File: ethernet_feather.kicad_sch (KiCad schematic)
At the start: 13 parts

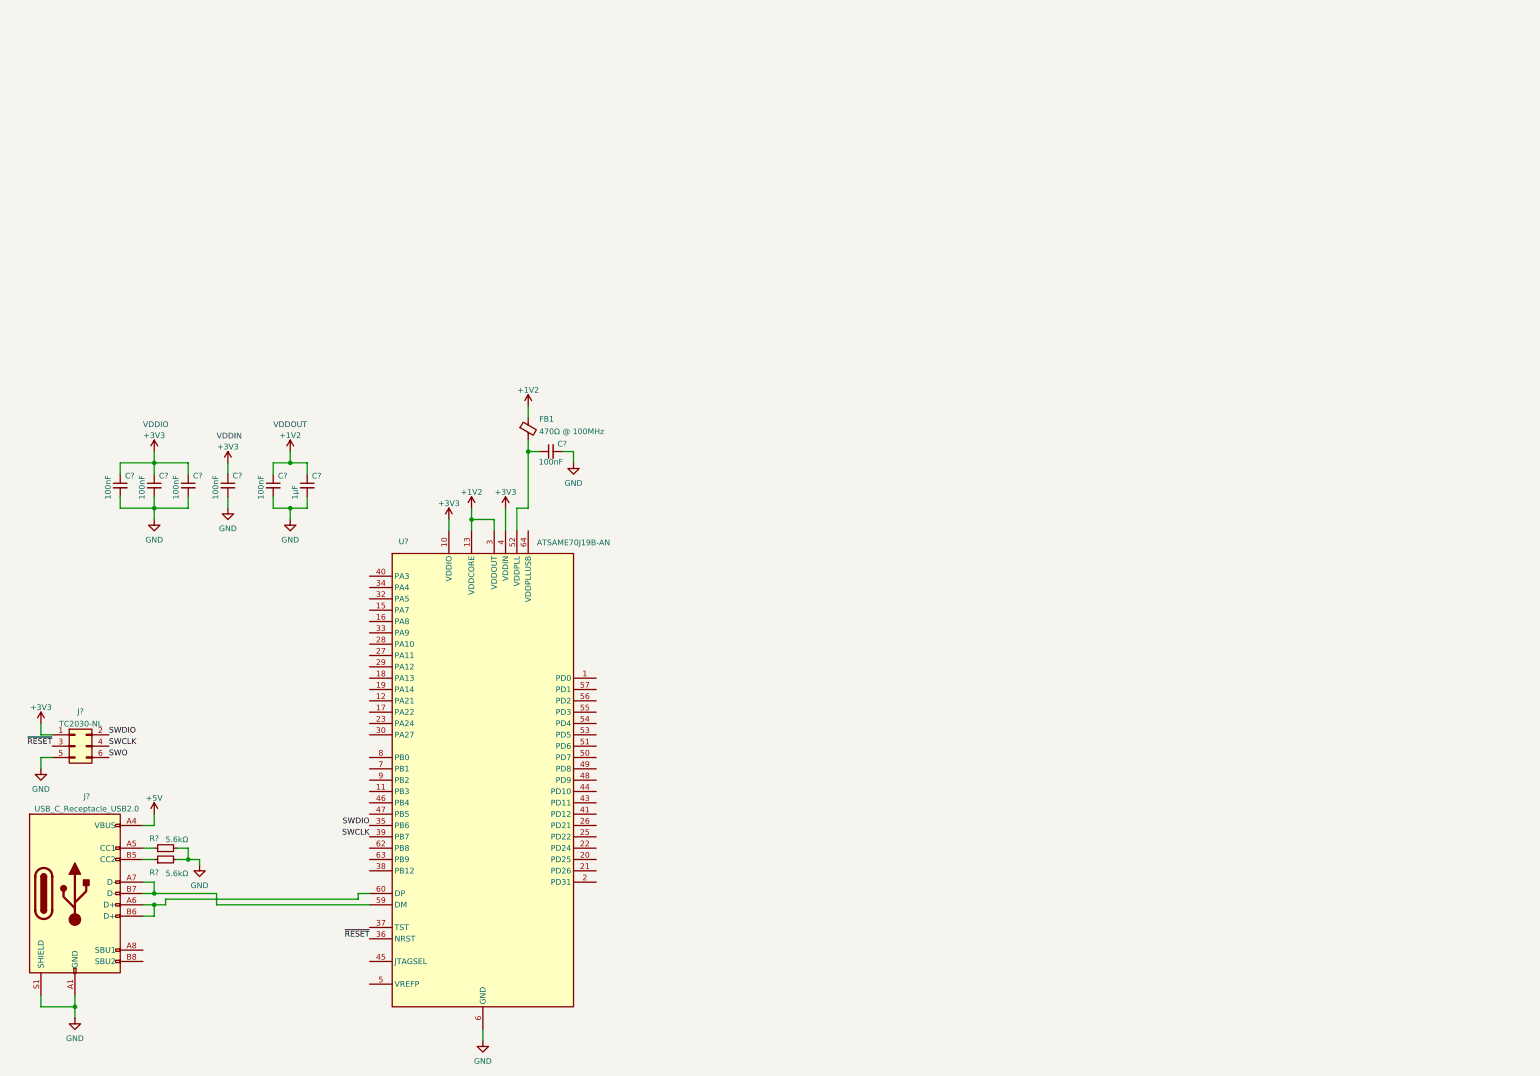
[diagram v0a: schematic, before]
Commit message: Add crystals
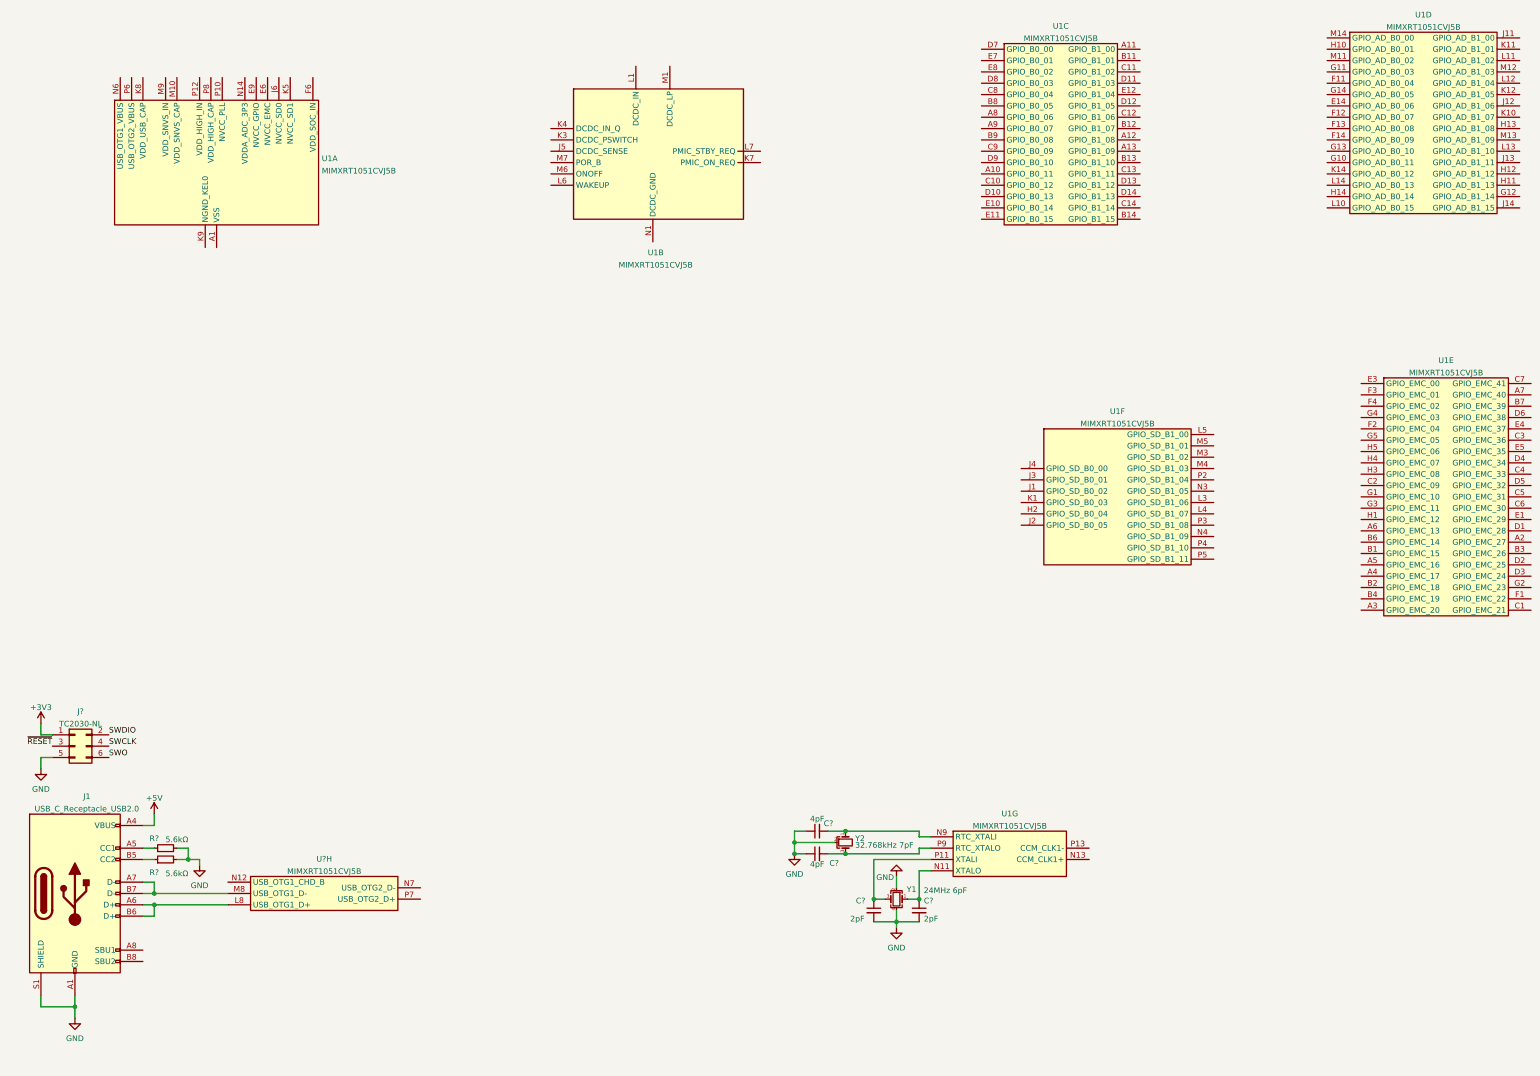
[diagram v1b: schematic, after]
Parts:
- removed C? (x6): 100nF, symbol Device:C_Small
- removed C?: 1µF, symbol Device:C_Small
- removed FB1: 470Ω @ 100MHz, symbol Device:FerriteBead_Small
- removed U?: ATSAME70J19B-AN, Package_QFP:LQFP-64_10x10mm_P0.5mm, symbol MCU_Microchip_SAME:ATSAME70J19A-AN
- added C? (x2): 4pF, symbol Device:C_Small
- added C? (x2): 2pF, Capacitor_SMD:C_0603_1608Metric, symbol Device:C_Small
- added U1, U?: MIMXRT1051CVJ5B, symbol ethernet_feather:MIMXRT1051CVJ5B
- added Y1: 24MHz 6pF, Crystal:Crystal_SMD_2016-4Pin_2.0x1.6mm, symbol Device:Crystal_GND24_Small
- added Y2: 32.768kHz 7pF, Crystal:Crystal_SMD_MicroCrystal_MS3V-T1R, symbol Device:Crystal_GND2_Small
- gave numbers to parts that had none: 1
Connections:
- net GND: now also C?.1, C?.1, C?.2, C?.2, Y1.2, Y1.4, Y2.2
- net at J1.A6 (D+), J1.B6 (D+): now also U?.L8 (USB_OTG1_D+)
- net at J1.A7 (D-), J1.B7 (D-): now also U?.M8 (USB_OTG1_D-)
- new net: C?.1, U1.N11 (XTALO), Y1.1
- new net: C?.2, U1.N9 (RTC_XTALI), Y2.1
- new net: C?.1, U1.P11 (XTALI), Y1.3
- new net: C?.2, U1.P9 (RTC_XTALO), Y2.3
- new net: U1.M1 (DCDC_LP), U1.M2 (DCDC_LP)
- new net DCDC_GND: U1.N1 (DCDC_GND), U1.N2 (DCDC_GND)
- new net DCDC_IN: U1.L1 (DCDC_IN), U1.L2 (DCDC_IN)
- new net NVCC_EMC: U1.E6 (NVCC_EMC), U1.F5 (NVCC_EMC)
- new net NVCC_GPIO: U1.E9 (NVCC_GPIO), U1.F10 (NVCC_GPIO), U1.J10 (NVCC_GPIO)
- new net VDD_SOC_IN: U1.F6 (VDD_SOC_IN), U1.F7 (VDD_SOC_IN), U1.F8 (VDD_SOC_IN), U1.F9 (VDD_SOC_IN), U1.G6 (VDD_SOC_IN), U1.G9 (VDD_SOC_IN), U1.H6 (VDD_SOC_IN), U1.H9 (VDD_SOC_IN), U1.J9 (VDD_SOC_IN)
- new net VSS: U1.A1 (VSS), U1.A14 (VSS), U1.B10 (VSS), U1.B5 (VSS), U1.E13 (VSS), U1.E2 (VSS), U1.G7 (VSS), U1.G8 (VSS), U1.H7 (VSS), U1.H8 (VSS), U1.J7 (VSS), U1.J8 (VSS), U1.K13 (VSS), U1.K2 (VSS), U1.L9 (VSS), U1.N5 (VSS), U1.N8 (VSS), U1.P1 (VSS), U1.P14 (VSS)
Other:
- note removed: "VDDIN"
- note removed: "VDDIO"
- note removed: "VDDOUT"

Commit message: Most of the HV side captured
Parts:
- added A1: Adafruit_Feather_Generic, Module:Adafruit_Feather, symbol MCU_Module:Adafruit_Feather_Generic
- added C? (x9): 100nF, symbol Device:C_Small
- added C? (x4): 4.7µF, symbol Device:C_Small
- added C?: 1µF, symbol Device:C_Small
- added C?: 220nF, symbol Device:C_Small
- added C?: C_Small, symbol Device:C_Small
- added H1, H2: 0.1", MountingHole:MountingHole_2.5mm_Pad, symbol Mechanical:MountingHole_Pad
- added H3, H4: 0.1", MountingHole:MountingHole_2.5mm, symbol Mechanical:MountingHole
- added J?: Conn_02x02_Odd_Even, symbol Connector_Generic:Conn_02x02_Odd_Even
- added J?: RJ45_Abracon_ARJM11D7-114-AB-EW2, ethernet_feather:RJ45_Abracon_ARJM11D7-114, symbol ethernet_feather:RJ45_Abracon_ARJM11D7-114-AB-EW2
- added U?: WE-TVS-82400102, Package_TO_SOT_SMD:SOT-23-6, symbol Power_Protection:WE-TVS-82400102
- added U?: W25Q32JVZP, Package_SON:WSON-8-1EP_6x5mm_P1.27mm_EP3.4x4.3mm, symbol Memory_Flash:W25Q32JVZP
- C3, C4: renamed from C?; footprint (none) -> Capacitor_SMD:C_0603_1608Metric
- J1: footprint (none) -> Connector_USB:USB_C_Receptacle_HRO_TYPE-C-31-M-12
- R1, R2: renamed from R?; footprint (none) -> Resistor_SMD:R_0603_1608Metric
- U1: footprint (none) -> ethernet_feather:LFBGA-196_12x12mm_Layout14x14_P0.8mm
- U1: renamed from U?; footprint (none) -> ethernet_feather:LFBGA-196_12x12mm_Layout14x14_P0.8mm
- gave numbers to parts that had none: 3
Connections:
- net NVCC_EMC is gone; now on net +3V3: U1.E6 (NVCC_EMC), U1.F5 (NVCC_EMC)
- net NVCC_GPIO is gone; now on net +3V3: U1.E9 (NVCC_GPIO), U1.F10 (NVCC_GPIO), U1.J10 (NVCC_GPIO)
- net VSS is gone; now on net GND: U1.A1 (VSS), U1.A14 (VSS), U1.B10 (VSS), U1.B5 (VSS), U1.E13 (VSS), U1.E2 (VSS), U1.G7 (VSS), U1.G8 (VSS), U1.H7 (VSS), U1.H8 (VSS), U1.J7 (VSS), U1.J8 (VSS), U1.K13 (VSS), U1.K2 (VSS), U1.L9 (VSS), U1.N5 (VSS), U1.N8 (VSS), U1.P1 (VSS), U1.P14 (VSS)
- net +3V3: now also U1.J6 (NVCC_SD0), U1.K5 (NVCC_SD1), U1.N14 (VDDA_ADC_3P3), U1.P12 (VDD_HIGH_IN), C?.1, C?.1, C?.1, C?.1, C?.1, C?.1, C?.1, C?.1, C?.1, C?.1, C?.1, C?.1, C?.1, U?.8 (VCC)
- net +5V: now also U?.5
- net GND: now also U1.K9 (NGND_KEL0), C?.1, C?.1, C?.2, C?.2, C?.2, C?.2, C?.2, C?.2, C?.2, C?.2, C?.2, C?.2, C?.2, C?.2, C?.2, H1.1, H2.1, J?.SH (SHIELD), U?.2, U?.4 (GND), U?.9 (EP)
- net SWDIO: now also U1.A8 (GPIO_B0_06)
- net SWO: now also U1.D10 (GPIO_B0_13)
- net ~{RESET}: now also U1.A10 (GPIO_B0_11)
- net SWDCLK: now reaches U1.A9 (GPIO_B0_07)
- net at J1.A6 (D+), J1.B6 (D+): now also U?.6; no longer U1.L8 (USB_OTG1_D+)
- net at J1.A7 (D-), J1.B7 (D-): now also U?.4; no longer U1.M8 (USB_OTG1_D-)
- net at U1.L3 (GPIO_SD_B1_06): now also U?.1 (~{CS})
- net at U1.L4 (GPIO_SD_B1_07): now also U?.6 (CLK)
- net at U1.N4 (GPIO_SD_B1_09): now also U?.2 (DO(IO1))
- net at U1.P3 (GPIO_SD_B1_08): now also U?.5 (DI(IO0))
- net at U1.P4 (GPIO_SD_B1_10): now also U?.3 (IO2)
- net at U1.P5 (GPIO_SD_B1_11): now also U?.7 (IO3)
- new net: C?.2, J?.4 (CT)
- new net: U1.L8 (USB_OTG1_D+), U?.1
- new net: U1.M8 (USB_OTG1_D-), U?.3
- new net: C?.2, J?.9 (V+)
- new net: J?.1 (Pin_1), J?.2 (TD-)
- new net: J?.2 (Pin_2), J?.7
- new net: J?.1 (TD+), J?.3 (Pin_3)
- new net: J?.4 (Pin_4), J?.6 (RD-)
- no-connect marks 0 -> 4
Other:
- moved on the sheet: C1, C2, C3, C4, J1, R1, R2, U1A, U1D, U1F, U1G, U1H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

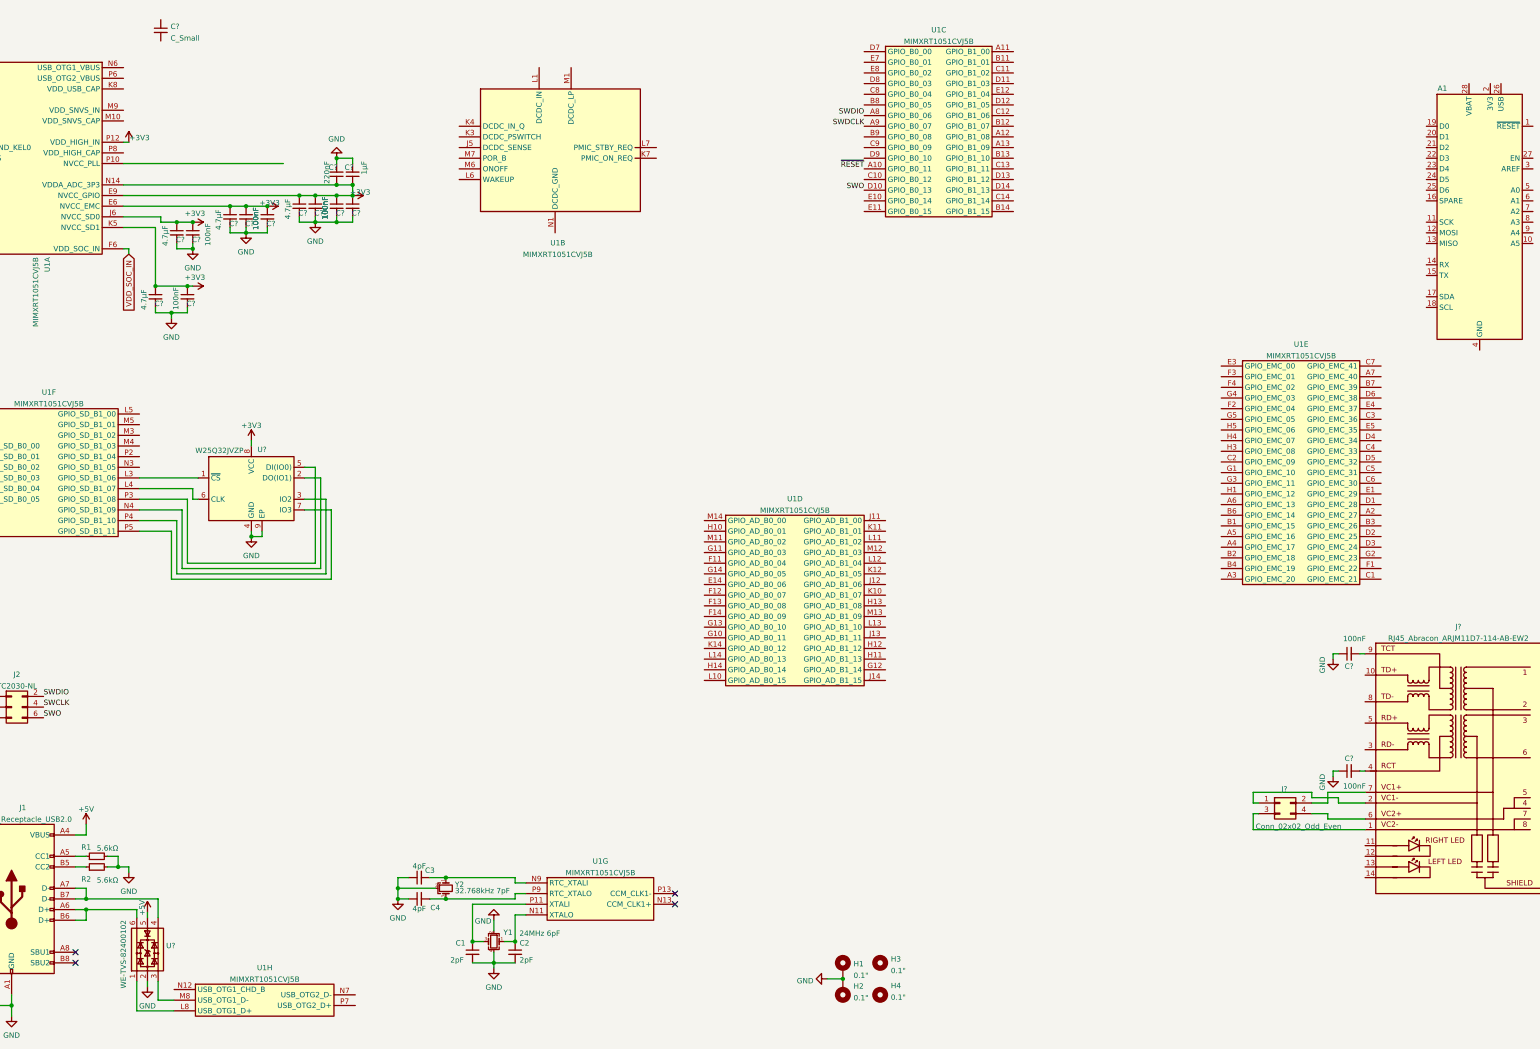
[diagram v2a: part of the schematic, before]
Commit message: Assign footprints and add LDO
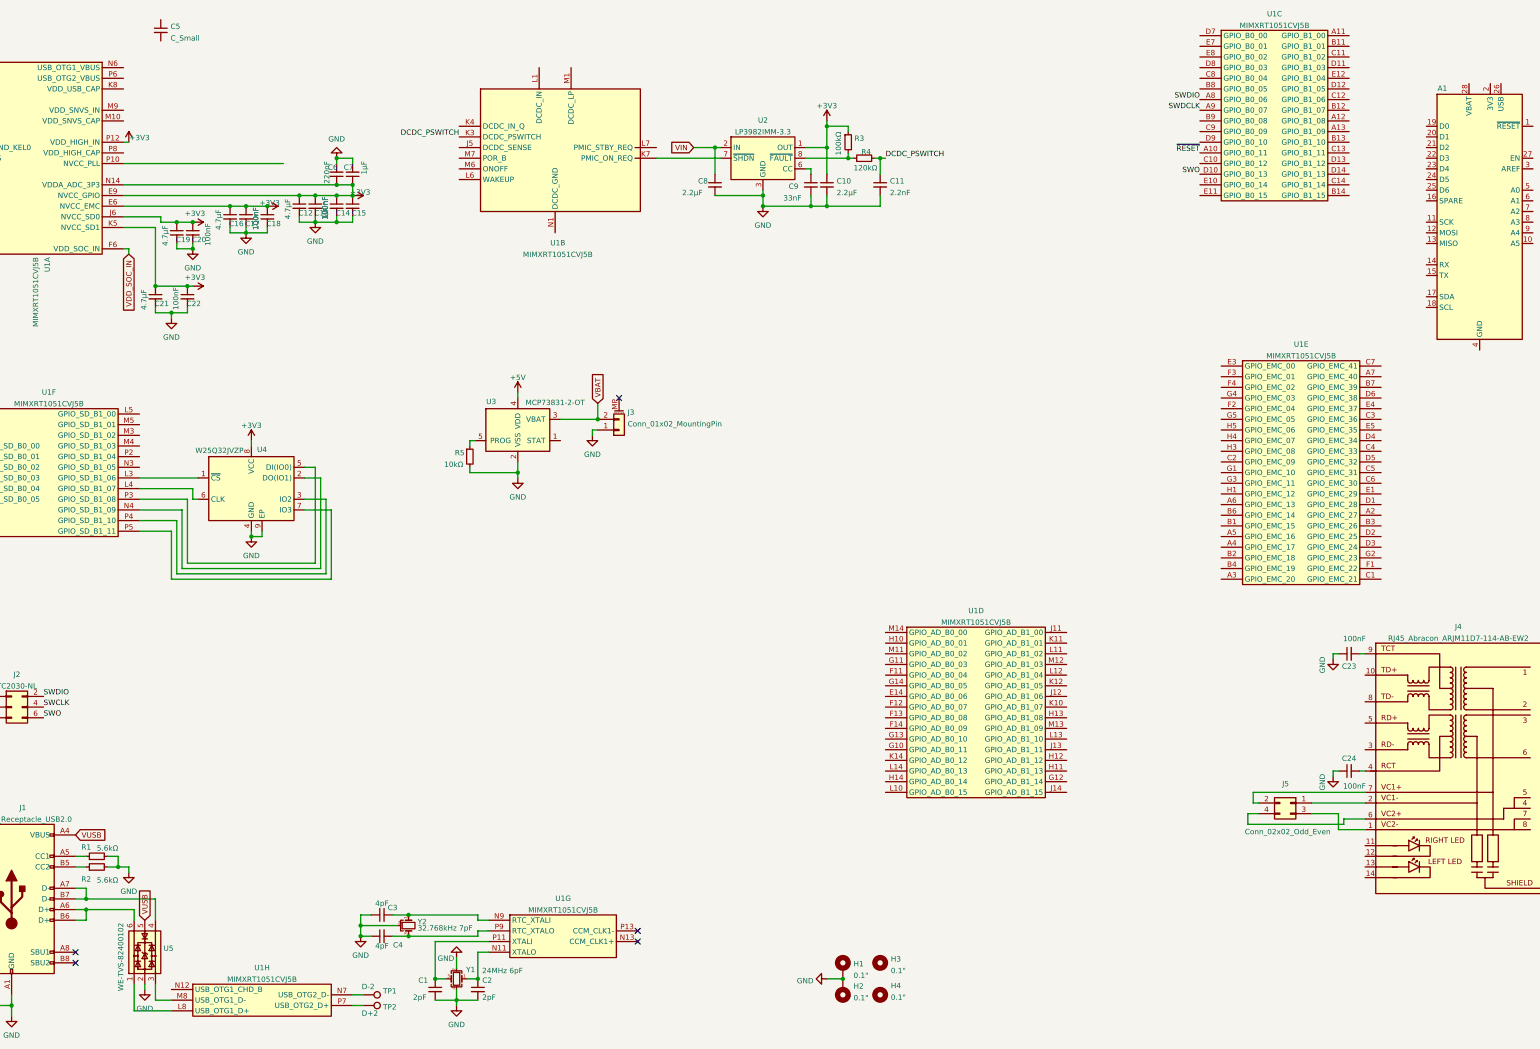
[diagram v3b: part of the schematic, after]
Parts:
- added C10, C8: 2.2µF, Capacitor_SMD:C_0603_1608Metric, symbol Device:C_Small
- added C11: 2.2nF, Capacitor_SMD:C_0603_1608Metric, symbol Device:C_Small
- added C9: 33nF, Capacitor_SMD:C_0603_1608Metric, symbol Device:C_Small
- added J3: Conn_01x02_MountingPin, Connector_JST:JST_PH_S2B-PH-SM4-TB_1x02-1MP_P2.00mm_Horizontal, symbol Connector_Generic_MountingPin:Conn_01x02_MountingPin
- added R3: 100kΩ, Resistor_SMD:R_0603_1608Metric, symbol Device:R_Small
- added R4: 120kΩ, Resistor_SMD:R_0603_1608Metric, symbol Device:R_Small
- added R5: 10kΩ, Resistor_SMD:R_0603_1608Metric, symbol Device:R_Small
- added TP1: D-2, TestPoint:TestPoint_Pad_D1.0mm, symbol Connector:TestPoint
- added TP2: D+2, TestPoint:TestPoint_Pad_D1.0mm, symbol Connector:TestPoint
- added U2: LP3982IMM-3.3, Package_SO:VSSOP-8_3.0x3.0mm_P0.65mm, symbol Regulator_Linear:LP3982IMM-3.3
- added U3: MCP73831-2-OT, Package_TO_SOT_SMD:SOT-23-5, symbol Battery_Management:MCP73831-2-OT
- C12, C13, C14, C15, C16, C17, C18, C19, C20, C21, C22, C23, C24, C5, C6, C7: renamed from C?; footprint (none) -> Capacitor_SMD:C_0603_1608Metric
- J5: renamed from J?; footprint (none) -> Connector_PinSocket_2.54mm:PinSocket_2x02_P2.54mm_Vertical
- gave numbers to parts that had none: 3
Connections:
- net +3V3: now also C10.1, R3.1, U2.1 (OUT), U2.4 (OUT)
- net +5V: now also U3.4 (VDD); no longer J1.A4 (VBUS), J1.A9 (VBUS), J1.B4 (VBUS), J1.B9 (VBUS), U5.5
- net GND: now also C10.2, C11.2, C8.2, C9.2, J3.1 (Pin_1), R5.2, U2.3 (GND), U3.2 (VSS)
- net at U1.N7 (USB_OTG2_D-): now also TP1.1
- net at U1.P7 (USB_OTG2_D+): now also TP2.1
- net DCDC_PSWITCH: now reaches U1.K3 (DCDC_PSWITCH)
- net DCDC_PSWITCH: now also C11.1, R4.2
- net at U1.K7 (PMIC_ON_REQ): now also U2.7 (~{SHDN})
- new net: C9.1, U2.6 (CC)
- new net: R5.1, U3.5 (PROG)
- new net: R3.2, R4.1, U2.8 (~{FAULT})
- new net VBAT: J3.2 (Pin_2), U3.3 (VBAT)
- new net VIN: C8.1, U2.2 (IN)
- new net VUSB: J1.A4 (VBUS), J1.A9 (VBUS), J1.B4 (VBUS), J1.B9 (VBUS), U5.5
- no-connect marks 4 -> 5
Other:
- moved on the sheet: C1, C2, C3, C4, U1C, U1D, U1G, U1H, U5, Y1, Y2

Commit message: Add some connectors
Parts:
- added C?: 100nF, symbol Device:C_Small
- added J4: JST SH4 pin, Connector_JST:JST_SH_SM04B-SRSS-TB_1x04-1MP_P1.00mm_Horizontal, symbol Connector_Generic_MountingPin:Conn_01x04_MountingPin
- added J?: Micro_SD_Card, symbol Connector:Micro_SD_Card
- added R? (x2): 10kΩ, symbol Device:R_Small
- J3: value Conn_01x02_MountingPin -> JST PH 2 pin
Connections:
- net +3V3: now also C?.1, J4.2 (Pin_2), R?.1, R?.1
- net GND: now also C?.2, J4.1 (Pin_1)
- new net QWIIC_SCL: J4.4 (Pin_4), R?.2
- new net QWIIC_SDA: J4.3 (Pin_3), R?.2
- no-connect marks 5 -> 6
